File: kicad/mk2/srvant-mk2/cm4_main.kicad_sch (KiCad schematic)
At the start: 58 parts, among them J10 HDMI connector, J11 USB A, J6 Conn_02x05_Odd_Even, J8 Bus_M.2_Socket_M, J9 ARJM11, U13 74AHC1G04, U14 AP22653W6, U16 FSUSB42MUX, U17 PCF85063AT/AAZ, U18 74LVC1G07SE-7, U19 TPD4EUSB30, U20 TPD4EUSB30, U21 74LVC1G07SE-7, U23 SLB9670VQ20FW785XTMA1, U25 74AHC1G08, Y3 X32K768S301

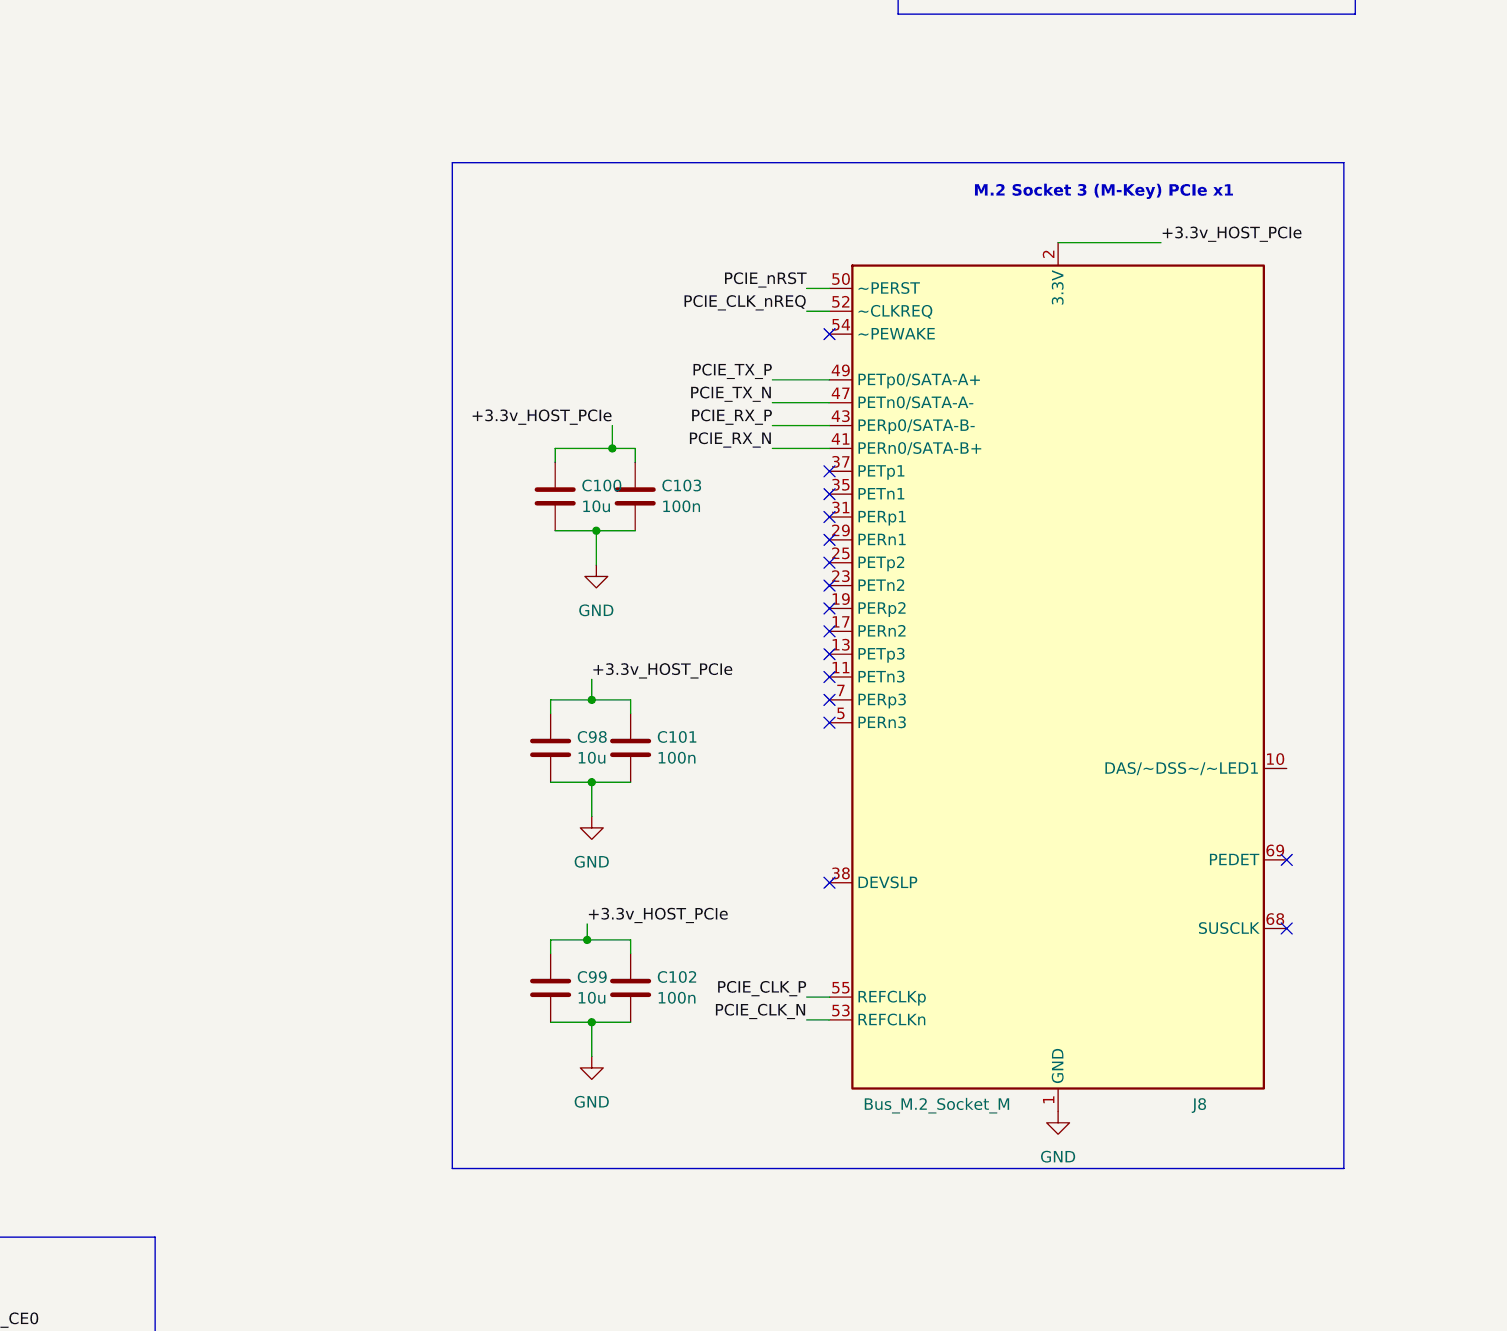
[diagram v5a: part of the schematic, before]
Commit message: replace power jack, change board dimentions, small fixes
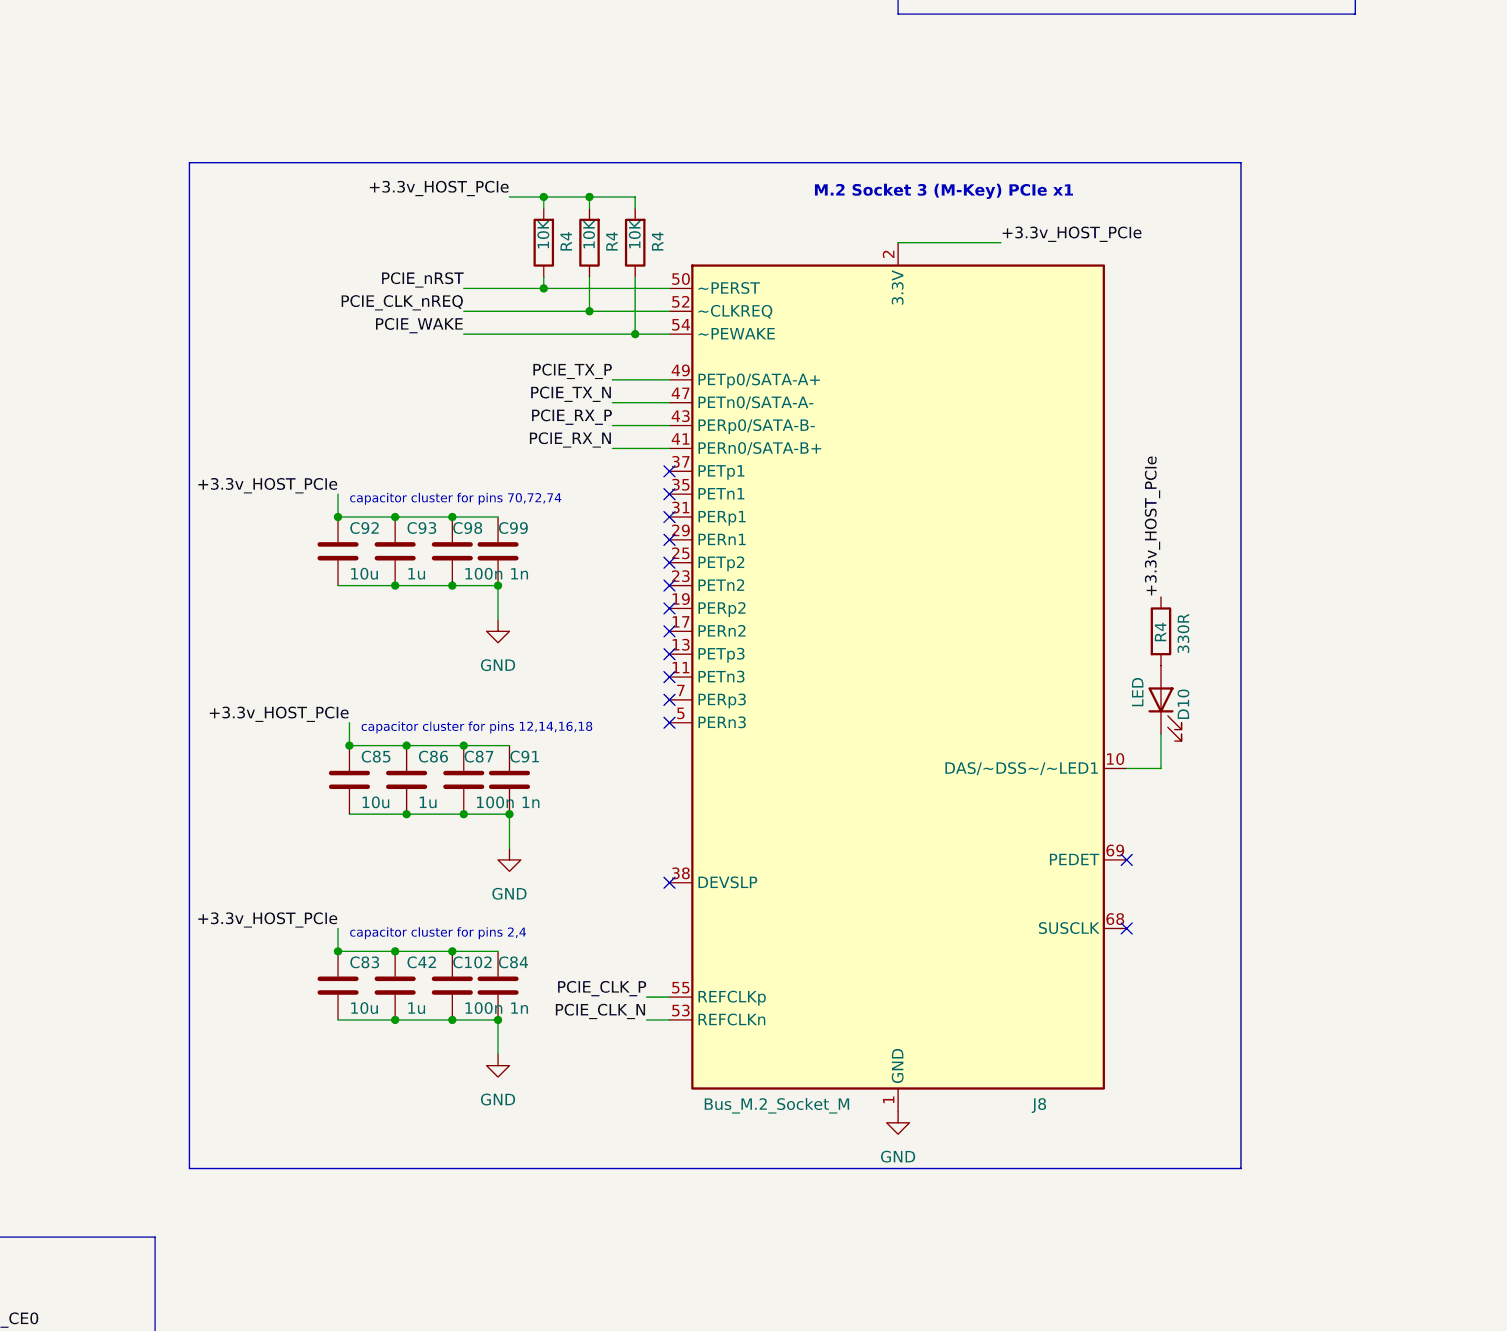
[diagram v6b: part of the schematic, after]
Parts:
- removed C100: 10u, Capacitor_SMD:C_0805_2012Metric, symbol Device:C
- removed C101, C103: 100n, Capacitor_SMD:C_0805_2012Metric, symbol Device:C
- added C42, C86, C93: 1u, Capacitor_SMD:C_0805_2012Metric, symbol Device:C
- added C83, C85, C92: 10u, Capacitor_SMD:C_0805_2012Metric, symbol Device:C
- added C84, C91: 1n, Capacitor_SMD:C_0805_2012Metric, symbol Device:C
- added C87: 100n, Capacitor_SMD:C_0805_2012Metric, symbol Device:C
- added D10: LED, LED_SMD:LED_0603_1608Metric, symbol Device:LED
- added R4 (x3): 10K, Resistor_SMD:R_0402_1005Metric, symbol Device:R
- added R4: 330R, Resistor_SMD:R_0402_1005Metric, symbol Device:R
- C98: value 10u -> 100n; Field4 Digikey -> Farnell; Field5 490-14381-1-ND -> 2611911; Field6 GRM21BR71A106KA73L -> RM EMK105 B7104KV-F; Field7 Murata -> TAIYO YUDEN EUROPE GMBH; Field8 111893011 -> 110091611; Part Description 10uF 10% 10V Ceramic Capacitor X7R 0805 (2012 Metric) -> 0.1uF 10% 16V Ceramic Capacitor X7R 0402 (1005 Metric)
- C99: value 10u -> 1n; Field4 Digikey -> (none); Field5 490-14381-1-ND -> (none); Field6 GRM21BR71A106KA73L -> (none); Field7 Murata -> (none); Field8 111893011 -> (none); Part Description 10uF 10% 10V Ceramic Capacitor X7R 0805 (2012 Metric) -> (none)
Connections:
- net +3.3v_HOST_PCIe: now also C42.1, C83.1, C84.1, C85.1, C86.1, C87.1, C91.1, C92.1, C93.1, R4.1, R4.2, R4.2, R4.2
- net GND: now also C42.2, C83.2, C84.2, C85.2, C86.2, C87.2, C91.2, C92.2, C93.2
- net PCIE_CLK_nREQ: now also R4.1
- net PCIE_nRST: now also R4.1
- net at J8.10 (DAS/~DSS~/~LED1): now also D10.1 (K)
- net PCIE_WAKE: now reaches J8.54 (~PEWAKE)
- net PCIE_WAKE: now also R4.1
- new net: D10.2 (A), R4.2
- no-connect marks 75 -> 74
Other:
- note added: "capacitor cluster for pins 12,14,16,18"
- note added: "capacitor cluster for pins 2,4"
- note added: "capacitor cluster for pins 70,72,74"
- moved on the sheet: C102, J8

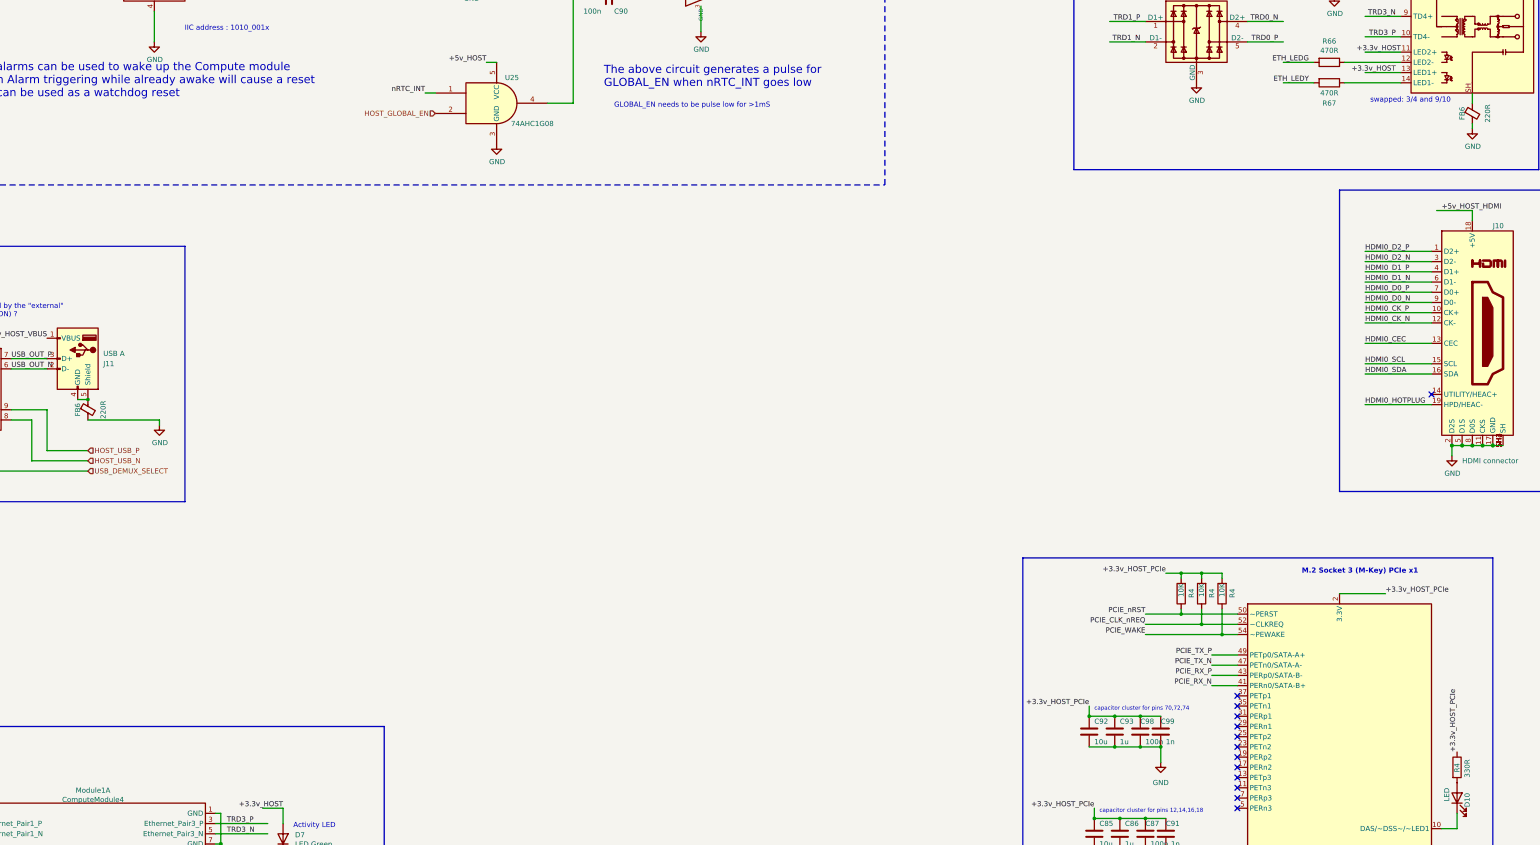
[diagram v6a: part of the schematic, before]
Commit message: add rp-t113-s3 datasheets (cn), make CI happier
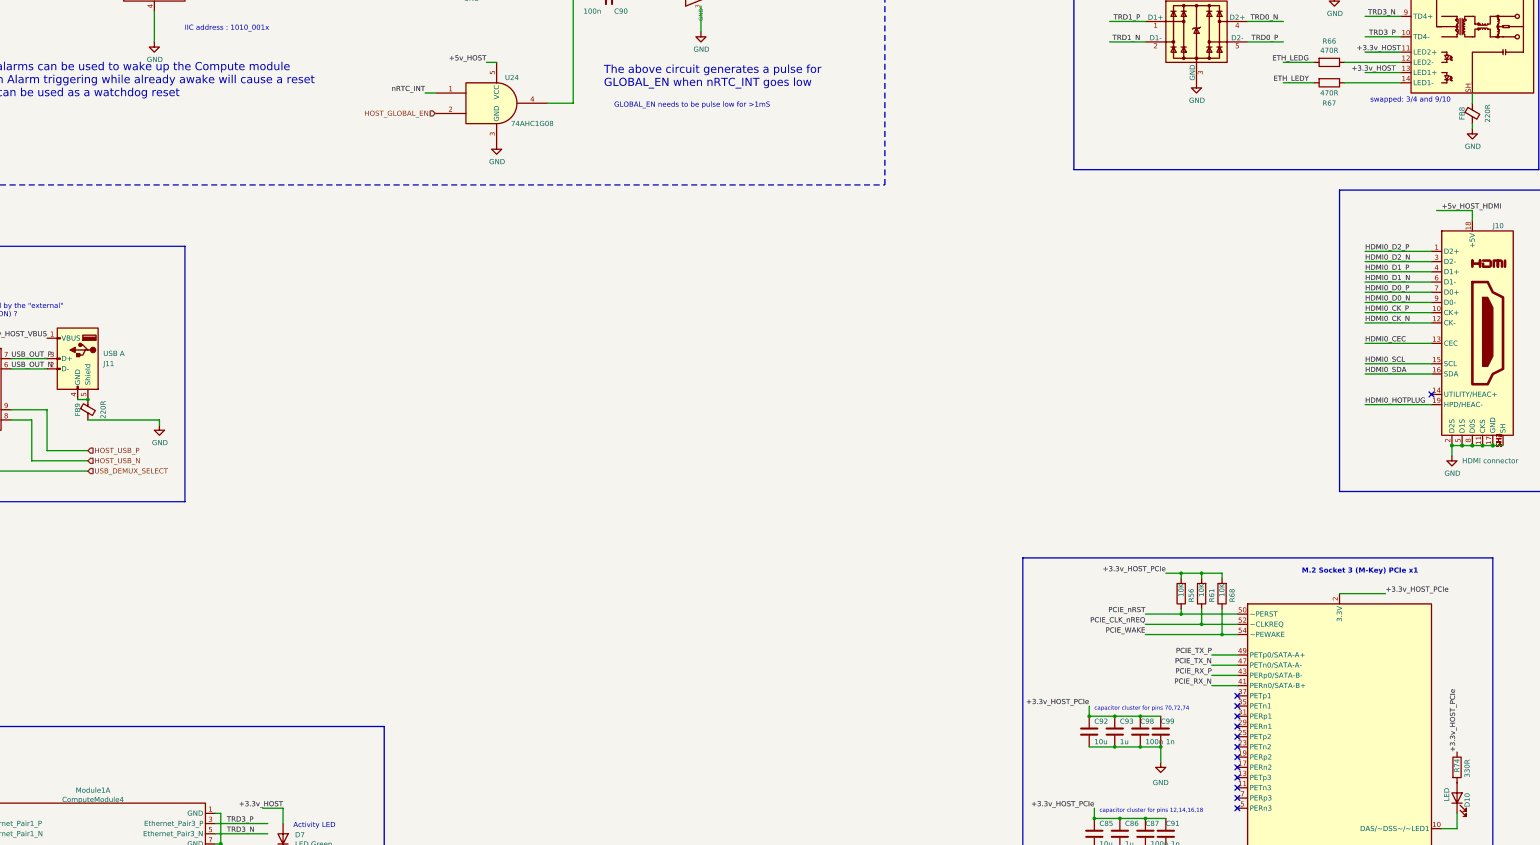
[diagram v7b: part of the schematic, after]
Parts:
- C70, C75, C77, C79, C81, C83, C85, C92: digikey# (none) -> 490-14381-1-ND; manf# (none) -> GRM21BR71A106KA73L
- C74: Field5 ECASD40J107M015K00 -> ECASD40J107M015K00
- D10, D8: Field4 Digikey -> Digikey; Field5 LTST-S270KRKT -> LTST-S270KRKT
- D7: Field4 Digikey -> Digikey
- FB8, FB9: renamed from FB6; manf# BLM15PX221SH1D -> BLM15PX221SH1D; mouser# 81-BLM15PX221SH1D -> 81-BLM15PX221SH1D
- J11: Part Description GSB19110KEU -> GSB19110KEU
- R58: Field6 RK73G1ETQTP2201D -> RK73G1ETQTP2201D
- R66, R67: Field6 RK73G1ETQTP4700D -> RK73G1ETQTP4700D
- U13: manf# SN74AHC1G04DBVRG4 -> SN74AHC1G04DBVRG4
- U14: Field5 31-AP22653W6-7CT-ND -> 31-AP22653W6-7CT-ND
- renumbered R4 to R56, R4 to R61, R4 to R68, R4 to R74, U25 to U24
